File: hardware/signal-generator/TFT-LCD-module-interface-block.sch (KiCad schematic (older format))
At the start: 5 parts

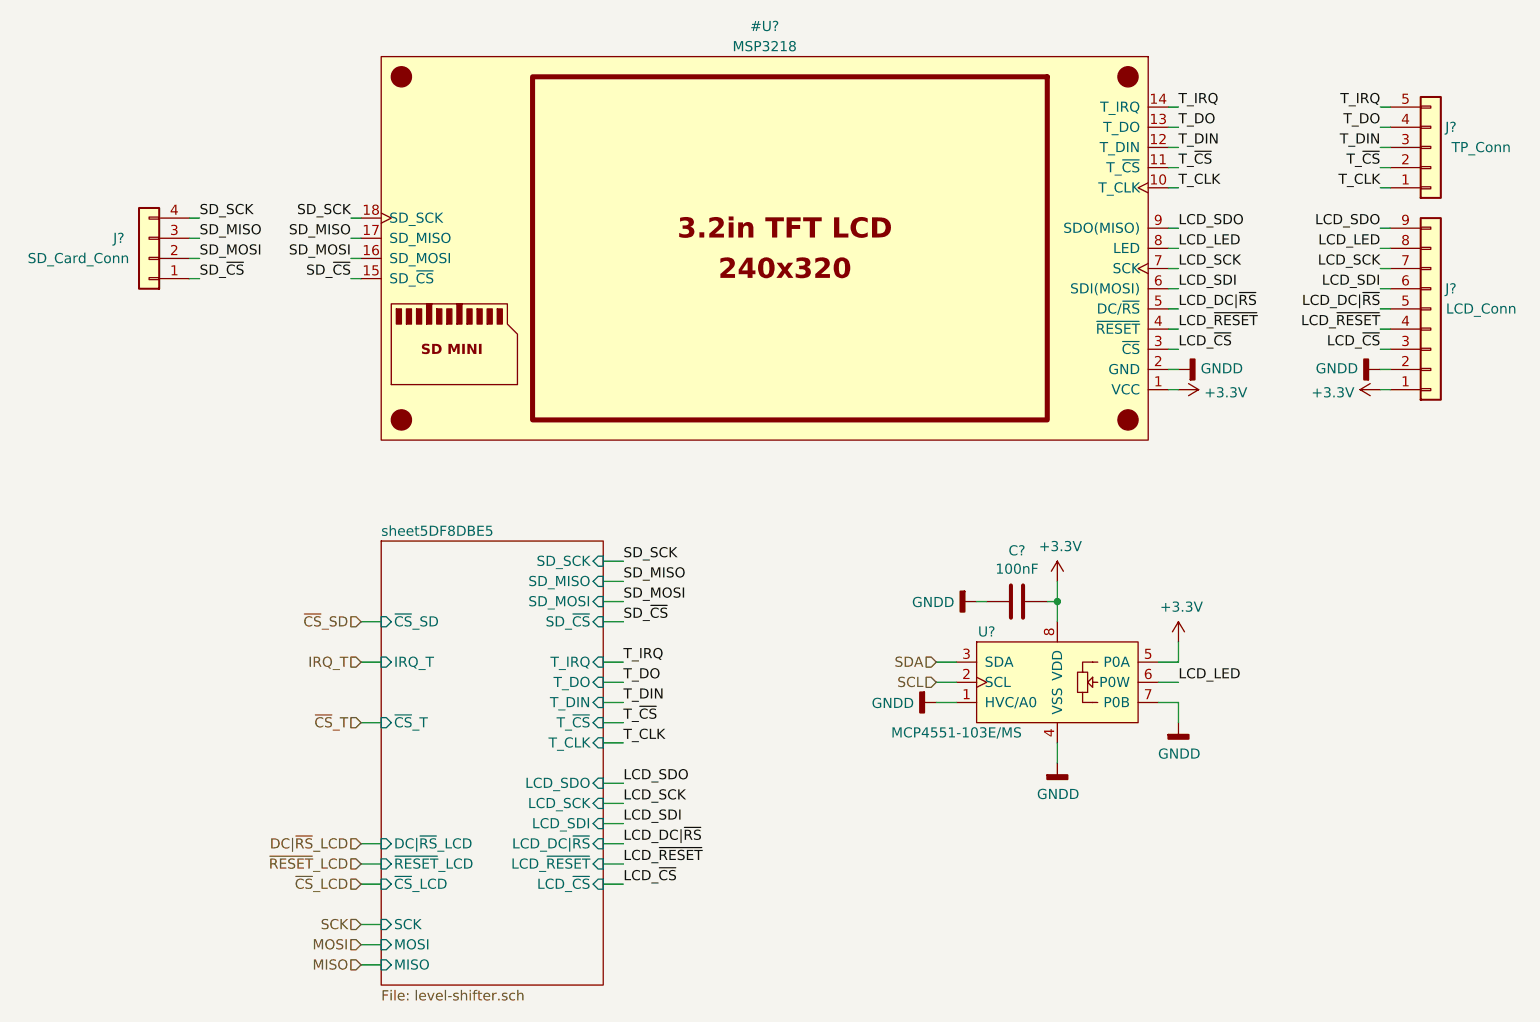
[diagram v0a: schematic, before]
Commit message: [Signal Generator] Layout microcontroller and allocate its pins
The microcontroller is the brains of the function generator system - it
is responsible for controlling the DDS signal generator system, as well
as the LCD module which provides the user interface. The specific
microcontroller used in this project is the ATmega2561-16AU from the
megaAVR uC family. The reasons I have picked this particular part are
the following:
- I am familiar with the AVR uC structure;
- it provides more SRAM memory (8 kB) than other MCUs of the same family;
- it has fewer pins (and therefore peripherals) than the ATmega2560.
Only a fraction of the available peripheral pins of the ATmega2561 have
been utilized in the current design. The remaining port pins (which are
internally connected to useful peripherals such as JTAG, XMEM, etc.)
are connected to pin header connectors and are meant for
upgrading/modifying the system as a whole by including additional
external circuitry. The ATmega2561's SPI port is also connected to a
similar pin header connector which allows the uC to play the role of an
SPI slave device.
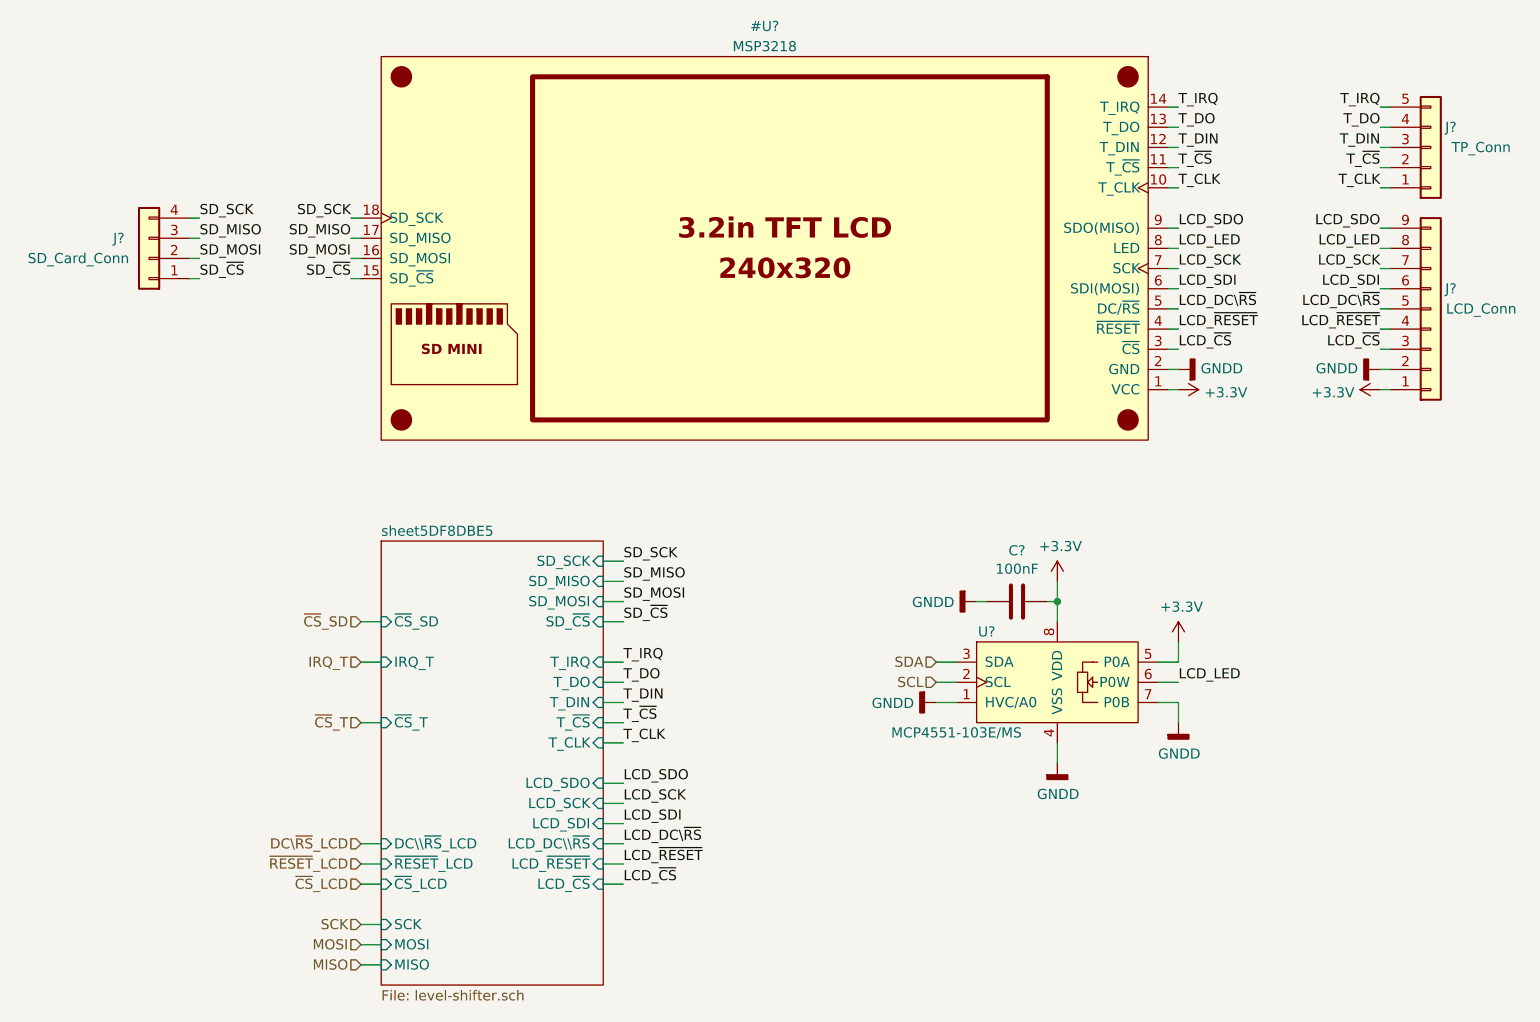
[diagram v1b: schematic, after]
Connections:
- net LCD_DC|~RS renamed LCD_DC\~RS
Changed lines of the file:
@@
 F8 "T_CLK" I R 4250 4800 50
 F9 "LCD_SCK" I R 4250 5100 50
-F10 "LCD_DC|~RS" I R 4250 5300 50
-F11 "SCK" I L 3150 5700 50
-F12 "MOSI" I L 3150 5800 50
-F13 "MISO" I L 3150 5900 50
-F14 "DC|~RS~_LCD" I L 3150 5300 50
-F15 "IRQ_T" I L 3150 4400 50
-F16 "LCD_SDO" I R 4250 5000 50
-F17 "LCD_SDI" I R 4250 5200 50
-F18 "SD_~CS" I R 4250 4200 50
-F19 "T_~CS" I R 4250 4700 50
-F20 "LCD_~RESET" I R 4250 5400 50
-F21 "~CS~_SD" I L 3150 4200 50
-F22 "~CS~_T" I L 3150 4700 50
-F23 "LCD_~CS" I R 4250 5500 50
-F24 "~CS~_LCD" I L 3150 5500 50
-F25 "~RESET~_LCD" I L 3150 5400 50
+F10 "SCK" I L 3150 5700 50
+F11 "MOSI" I L 3150 5800 50
+F12 "MISO" I L 3150 5900 50
+F13 "IRQ_T" I L 3150 4400 50
+F14 "LCD_SDO" I R 4250 5000 50
+F15 "LCD_SDI" I R 4250 5200 50
+F16 "SD_~CS" I R 4250 4200 50
+F17 "T_~CS" I R 4250 4700 50
+F18 "LCD_~RESET" I R 4250 5400 50
+F19 "~CS~_SD" I L 3150 4200 50
+F20 "~CS~_T" I L 3150 4700 50
+F21 "LCD_~CS" I R 4250 5500 50
+F22 "~CS~_LCD" I L 3150 5500 50
+F23 "~RESET~_LCD" I L 3150 5400 50
+F24 "LCD_DC\\~RS" I R 4250 5300 50
+F25 "DC\\~RS~_LCD" I L 3150 5300 50
 $EndSheet
 $Comp
@@
 LCD_SDI
 Text Label 7100 2650 0    50   ~ 0
-LCD_DC|~RS
+LCD_DC\~RS
 Text Label 7100 2750 0    50   ~ 0
 LCD_~RESET
@@
 LCD_SDI
 Text Label 4350 5300 0    50   ~ 0
-LCD_DC|~RS
+LCD_DC\~RS
 Text Label 4350 5400 0    50   ~ 0
 LCD_~RESET
@@
 LCD_SDI
 Text Label 8100 2650 2    50   ~ 0
-LCD_DC|~RS
+LCD_DC\~RS
 Text Label 8100 2750 2    50   ~ 0
 LCD_~RESET
@@
 MISO
 Text HLabel 3050 5300 0    50   Input ~ 0
-DC|~RS~_LCD
+DC\~RS~_LCD
 Text HLabel 3050 5400 0    50   Input ~ 0
 ~RESET~_LCD

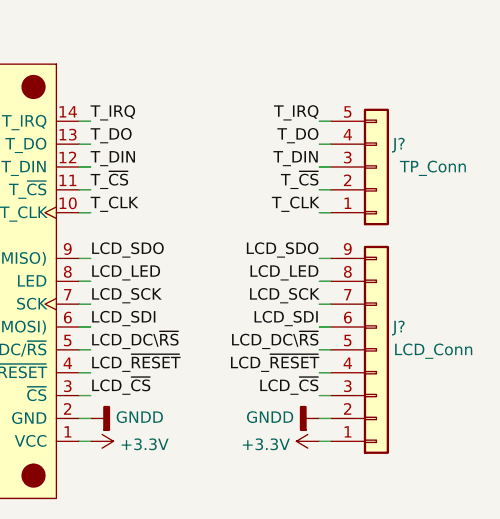
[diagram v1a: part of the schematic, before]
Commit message: [Signal Generator] Implement +3.3VD line with TC1017 voltage regulator
Up until now, the +3.3VD line was implemented using the L78L33 linear
voltage regulator. However, the latter has a dropout voltage of 2V which
means that the L78L33 cannot output a stable +3.3V from a +5V input.

To solve the aforementioned problem the TC1017 LDO voltage regulator has
replaced the L78L33. The former has a low dropout voltage of 180mV (typ.) at
100mA load current.
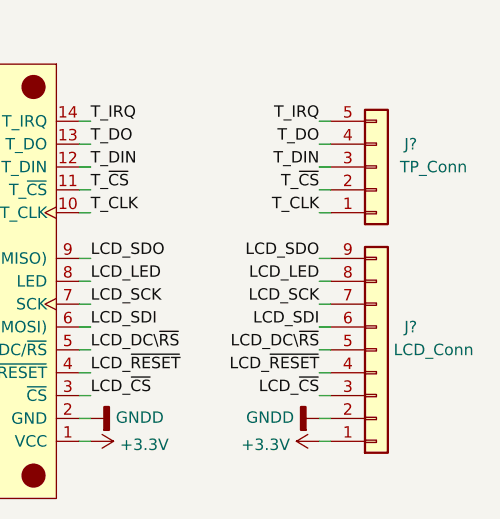
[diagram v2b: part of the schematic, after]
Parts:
- C?: footprint (none) -> Capacitors_SMD:C_1206_HandSoldering
- J?: footprint (none) -> Pin_Headers:Pin_Header_Straight_1x09_Pitch2.54mm
- J?: footprint (none) -> Pin_Headers:Pin_Header_Straight_1x05_Pitch2.54mm
- J?: footprint (none) -> Pin_Headers:Pin_Header_Straight_1x04_Pitch2.54mm
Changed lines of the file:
@@
 P 7100 3050
 AR Path="/5DF8DC0E" Ref="#PWR?"  Part="1"
-AR Path="/5DF89F54/5DF8DC0E" Ref="#PWR?"  Part="1"
-F 0 "#PWR?" H 7100 2900 50  0001 C CNN
+AR Path="/5DF89F54/5DF8DC0E" Ref="#PWR0218"  Part="1"
+F 0 "#PWR0218" H 7100 2900 50  0001 C CNN
 F 1 "+3.3V" V 7115 3178 50  0000 L CNN
 F 2 "" H 7100 3050 50  0001 C CNN
@@
 P 7100 2950
 AR Path="/5DF8DC14" Ref="#PWR?"  Part="1"
-AR Path="/5DF89F54/5DF8DC14" Ref="#PWR?"  Part="1"
-F 0 "#PWR?" H 7100 2700 50  0001 C CNN
+AR Path="/5DF89F54/5DF8DC14" Ref="#PWR0219"  Part="1"
+F 0 "#PWR0219" H 7100 2700 50  0001 C CNN
 F 1 "GNDD" V 7104 2840 50  0000 R CNN
 F 2 "" H 7100 2950 50  0001 C CNN
@@
 P 5900 4600
 AR Path="/5DF8DC75" Ref="#PWR?"  Part="1"
-AR Path="/5DF89F54/5DF8DC75" Ref="#PWR?"  Part="1"
-F 0 "#PWR?" H 5900 4350 50  0001 C CNN
+AR Path="/5DF89F54/5DF8DC75" Ref="#PWR0220"  Part="1"
+F 0 "#PWR0220" H 5900 4350 50  0001 C CNN
 F 1 "GNDD" V 5904 4490 50  0000 R CNN
 F 2 "" H 5900 4600 50  0001 C CNN
@@
 P 6500 4900
 AR Path="/5DF8DC7C" Ref="#PWR?"  Part="1"
-AR Path="/5DF89F54/5DF8DC7C" Ref="#PWR?"  Part="1"
-F 0 "#PWR?" H 6500 4650 50  0001 C CNN
+AR Path="/5DF89F54/5DF8DC7C" Ref="#PWR0221"  Part="1"
+F 0 "#PWR0221" H 6500 4650 50  0001 C CNN
 F 1 "GNDD" H 6504 4745 50  0000 C CNN
 F 2 "" H 6500 4900 50  0001 C CNN
@@
 F 0 "C?" V 6048 4100 50  0000 C CNN
 F 1 "100nF" V 6139 4100 50  0000 C CNN
-F 2 "" H 6338 3950 50  0001 C CNN
+F 2 "Capacitors_SMD:C_1206_HandSoldering" H 6338 3950 50  0001 C CNN
 F 3 "~" H 6300 4100 50  0001 C CNN
 	1    6300 4100
@@
 P 6100 4100
 AR Path="/5DF8DC8E" Ref="#PWR?"  Part="1"
-AR Path="/5DF89F54/5DF8DC8E" Ref="#PWR?"  Part="1"
-F 0 "#PWR?" H 6100 3850 50  0001 C CNN
+AR Path="/5DF89F54/5DF8DC8E" Ref="#PWR0222"  Part="1"
+F 0 "#PWR0222" H 6100 3850 50  0001 C CNN
 F 1 "GNDD" V 6104 3990 50  0000 R CNN
 F 2 "" H 6100 4100 50  0001 C CNN
@@
 P 6500 4000
 AR Path="/5DF8DC94" Ref="#PWR?"  Part="1"
-AR Path="/5DF89F54/5DF8DC94" Ref="#PWR?"  Part="1"
-F 0 "#PWR?" H 6500 3850 50  0001 C CNN
+AR Path="/5DF89F54/5DF8DC94" Ref="#PWR0223"  Part="1"
+F 0 "#PWR0223" H 6500 3850 50  0001 C CNN
 F 1 "+3.3V" H 6515 4173 50  0000 C CNN
 F 2 "" H 6500 4000 50  0001 C CNN
@@
 P 7100 4300
 AR Path="/5DF8DC9C" Ref="#PWR?"  Part="1"
-AR Path="/5DF89F54/5DF8DC9C" Ref="#PWR?"  Part="1"
-F 0 "#PWR?" H 7100 4150 50  0001 C CNN
+AR Path="/5DF89F54/5DF8DC9C" Ref="#PWR0224"  Part="1"
+F 0 "#PWR0224" H 7100 4150 50  0001 C CNN
 F 1 "+3.3V" H 7115 4473 50  0000 C CNN
 F 2 "" H 7100 4300 50  0001 C CNN
@@
 P 7100 4700
 AR Path="/5DF8DCA4" Ref="#PWR?"  Part="1"
-AR Path="/5DF89F54/5DF8DCA4" Ref="#PWR?"  Part="1"
-F 0 "#PWR?" H 7100 4450 50  0001 C CNN
+AR Path="/5DF89F54/5DF8DCA4" Ref="#PWR0225"  Part="1"
+F 0 "#PWR0225" H 7100 4450 50  0001 C CNN
 F 1 "GNDD" H 7104 4545 50  0000 C CNN
 F 2 "" H 7100 4700 50  0001 C CNN
@@
 P 8100 3050
 AR Path="/5DF8DCB5" Ref="#PWR?"  Part="1"
-AR Path="/5DF89F54/5DF8DCB5" Ref="#PWR?"  Part="1"
-F 0 "#PWR?" H 8100 2900 50  0001 C CNN
+AR Path="/5DF89F54/5DF8DCB5" Ref="#PWR0226"  Part="1"
+F 0 "#PWR0226" H 8100 2900 50  0001 C CNN
 F 1 "+3.3V" V 8115 3178 50  0000 L CNN
 F 2 "" H 8100 3050 50  0001 C CNN
@@
 P 8100 2950
 AR Path="/5DF8DCBB" Ref="#PWR?"  Part="1"
-AR Path="/5DF89F54/5DF8DCBB" Ref="#PWR?"  Part="1"
-F 0 "#PWR?" H 8100 2700 50  0001 C CNN
+AR Path="/5DF89F54/5DF8DCBB" Ref="#PWR0227"  Part="1"
+F 0 "#PWR0227" H 8100 2700 50  0001 C CNN
 F 1 "GNDD" V 8104 2840 50  0000 R CNN
 F 2 "" H 8100 2950 50  0001 C CNN
@@
 U 1 1 5DFB8DFB
 P 8350 2650
-F 0 "J?" H 8450 2550 50  0000 C CNN
+F 0 "J?" H 8500 2550 50  0000 C CNN
 F 1 "LCD_Conn" H 8600 2650 50  0000 C CNN
-F 2 "" H 8350 2650 50  0001 C CNN
+F 2 "Pin_Headers:Pin_Header_Straight_1x09_Pitch2.54mm" H 8350 2650 50  0001 C CNN
 F 3 "~" H 8350 2650 50  0001 C CNN
 	1    8350 2650
@@
 U 1 1 5DFB8ED1
 P 8350 1850
-F 0 "J?" H 8450 1750 50  0000 C CNN
+F 0 "J?" H 8500 1750 50  0000 C CNN
 F 1 "TP_Conn" H 8600 1850 50  0000 C CNN
-F 2 "" H 8350 1850 50  0001 C CNN
+F 2 "Pin_Headers:Pin_Header_Straight_1x05_Pitch2.54mm" H 8350 1850 50  0001 C CNN
 F 3 "~" H 8350 1850 50  0001 C CNN
 	1    8350 1850
@@
 F 0 "J?" H 2150 2300 50  0000 C CNN
 F 1 "SD_Card_Conn" H 2350 2400 50  0000 C CNN
-F 2 "" H 2000 2400 50  0001 C CNN
+F 2 "Pin_Headers:Pin_Header_Straight_1x04_Pitch2.54mm" H 2000 2400 50  0001 C CNN
 F 3 "~" H 2000 2400 50  0001 C CNN
 	1    2000 2400

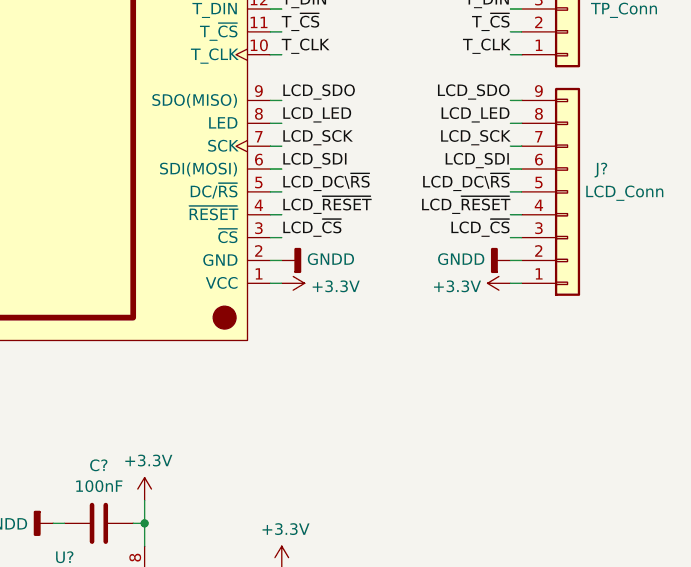
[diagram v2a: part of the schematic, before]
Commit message: [Signal Generator] Power the LCD module with the +5VD rail
Previously, the LCD module was powered via the +3.3VD rail. The module itself
consumes about 90mA and the level shifters may consume  >= 50mA in worst
case scenarios. Looking at the module's (MSP3218) schematic, it can be
observed that the VCC line is connected to the XC6206 +3.3V LDO voltage
regulator. Therefore, I have decided to power the module from the +5VD
supply rail which is external to the board (as opposed to the +3.3VD
rail which resides entirely on the digital function generator's PCB).
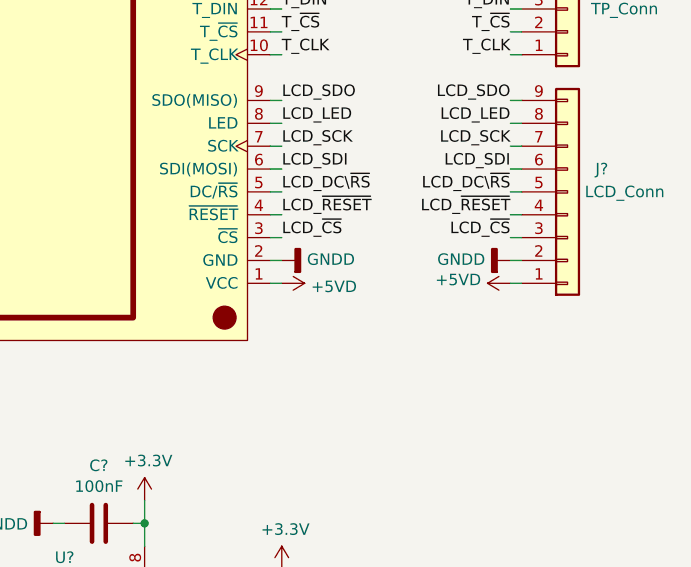
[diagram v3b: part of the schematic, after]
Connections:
- net +3V3: no longer J?.1 (Pin_1)
- new net +5VD: J?.1 (Pin_1)
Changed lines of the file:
@@
 Sheet 5 6
 Title "Digital Function Generator v2 - TFT LCD Module Interface Block"
-Date "2019-12-01"
+Date "2019-12-14"
 Rev "1"
 Comp "Petar Nikolov"
@@
 	7050 3050 7100 3050
 $Comp
-L power:+3.3V #PWR?
-U 1 1 5DF8DC0E
-P 7100 3050
-AR Path="/5DF8DC0E" Ref="#PWR?"  Part="1"
-AR Path="/5DF89F54/5DF8DC0E" Ref="#PWR0218"  Part="1"
-F 0 "#PWR0218" H 7100 2900 50  0001 C CNN
-F 1 "+3.3V" V 7115 3178 50  0000 L CNN
-F 2 "" H 7100 3050 50  0001 C CNN
-F 3 "" H 7100 3050 50  0001 C CNN
-	1    7100 3050
-	0    1    1    0
-$EndComp
-$Comp
 L power:GNDD #PWR?
 U 1 1 5DF8DC14
@@
 LCD_LED
 $Comp
-L power:+3.3V #PWR?
-U 1 1 5DF8DCB5
-P 8100 3050
-AR Path="/5DF8DCB5" Ref="#PWR?"  Part="1"
-AR Path="/5DF89F54/5DF8DCB5" Ref="#PWR0226"  Part="1"
-F 0 "#PWR0226" H 8100 2900 50  0001 C CNN
-F 1 "+3.3V" V 8115 3178 50  0000 L CNN
-F 2 "" H 8100 3050 50  0001 C CNN
-F 3 "" H 8100 3050 50  0001 C CNN
-	1    8100 3050
-	0    -1   1    0
-$EndComp
-$Comp
 L power:GNDD #PWR?
 U 1 1 5DF8DCBB
@@
 Text HLabel 3050 4200 0    50   Input ~ 0
 ~CS~_SD
+$Comp
+L power:+5VD #PWR?
+U 1 1 5E0A0514
+P 8100 3050
+F 0 "#PWR?" H 8100 2900 50  0001 C CNN
+F 1 "+5VD" V 8115 3178 50  0000 L CNN
+F 2 "" H 8100 3050 50  0001 C CNN
+F 3 "" H 8100 3050 50  0001 C CNN
+	1    8100 3050
+	0    -1   -1   0
+$EndComp
+$Comp
+L power:+5VD #PWR?
+U 1 1 5E0A0544
+P 7100 3050
+F 0 "#PWR?" H 7100 2900 50  0001 C CNN
+F 1 "+5VD" V 7115 3178 50  0000 L CNN
+F 2 "" H 7100 3050 50  0001 C CNN
+F 3 "" H 7100 3050 50  0001 C CNN
+	1    7100 3050
+	0    1    1    0
+$EndComp
 $EndSCHEMATC
